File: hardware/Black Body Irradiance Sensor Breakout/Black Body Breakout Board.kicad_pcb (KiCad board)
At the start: 2 copper layers, 15 x 13 mm, 6 parts, among them J2 Conn_01x05, U1 TSL25911FN

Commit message: actual irrad board update
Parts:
- moved C1 3.26 mm to (133.2, 72.8)
- moved R3 2.47 mm to (130.7, 71.3), turned to -90 degrees
- moved R2 1.82 mm to (125.5, 71.4)
- moved U1 1.69 mm to (128.1, 72.9)
- moved R1 0.34 mm to (123.3, 73.2)
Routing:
- net +3V3: track 3.93 -> 0.00 mm, vias 2 -> 0
- net Net-(J2-Pin_3): track 10.3 -> 7.15 mm
- net Net-(J2-Pin_4): track 8.38 -> 6.76 mm, vias 2 -> 1
- net Net-(J2-Pin_5): track 6.66 -> 7.81 mm

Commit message: updated irrad board
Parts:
- moved R2 2.70 mm to (127.5, 69.5)
- moved R3 0.55 mm to (130.8, 71.8), turned to 90 degrees
- moved C1 0.50 mm to (133.8, 72.8)
- moved R1 0.48 mm to (123.7, 72.9), turned to 0 degrees
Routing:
- net Net-(J2-Pin_3): track 7.15 -> 13.0 mm, vias 0 -> 1
- net +3V3: track 0.00 -> 5.43 mm
- net Net-(J2-Pin_4): track 6.76 -> 7.91 mm
- net GND: track 10.2 -> 10.9 mm, vias 2 -> 0
- net Net-(J2-Pin_5): track 7.81 -> 7.80 mm, vias 0 -> 1

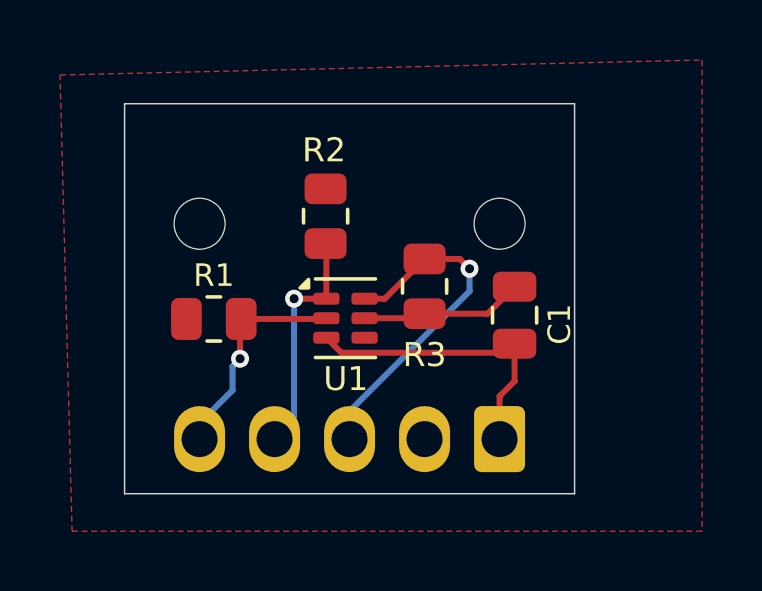
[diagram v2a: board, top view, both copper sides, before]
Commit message: updated fuse silkscreen, added open circuit to TC
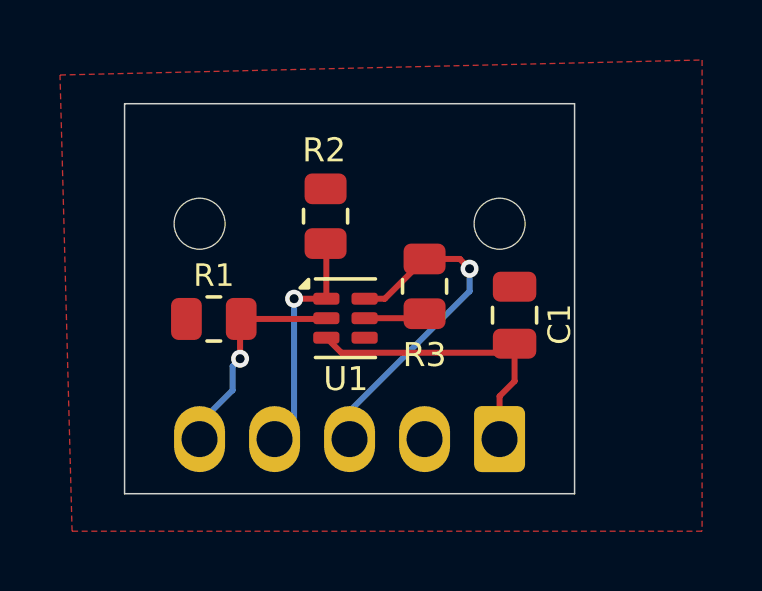
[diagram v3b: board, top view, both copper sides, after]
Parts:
- R2, R3: value 1.5k -> 10k
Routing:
- net +3V3: track 5.43 -> 2.06 mm
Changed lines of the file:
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@@
 			)
 		)
-		(property "Value" "1.5k"
+		(property "Value" "10k"
 			(at 0 1.65 90)
 			(layer "F.Fab")
@@
 			)
 		)
-		(property "Value" "1.5k"
+		(property "Value" "10k"
 			(at 0 1.65 90)
 			(layer "F.Fab")
@@
 		(width 0.2)
 		(layer "F.Cu")
-		(net 1)
-	)
-	(segment
-		(start 130.75 72.75)
-		(end 132.85 72.75)
-		(width 0.2)
-		(layer "F.Cu")
-		(net 1)
-	)
-	(segment
-		(start 132.85 72.75)
-		(end 133.75 71.85)
-		(width 0.2)
-		(layer "F.Cu")

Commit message: updated cap
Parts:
- C1: footprint Capacitor_SMD:C_0805_2012Metric -> Capacitor_SMD:C_0201_0603Metric_Pad0.64x0.40mm_HandSolder
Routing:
- net GND: track 10.9 -> 11.5 mm
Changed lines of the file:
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@@
+			)
+		)
+		(property "LCSC" "C25804"
+			(at 0 0 0)
+			(layer "F.SilkS")
+			(hide yes)
+			(effects
+				(font
+					(size 1.27 1.27)
+					(thickness 0.15)
+				)
 			)
 		)
@@
 			)
 		)
+		(property "LCSC" "C25804"
+			(at 0 0 0)
+			(layer "F.SilkS")
+			(hide yes)
+			(effects
+				(font
+					(size 1.27 1.27)
+					(thickness 0.15)
+				)
+			)
+		)
 		(property ki_fp_filters "R_*")
 		(sheetname "/")
@@
 			)
 		)
+		(property "LCSC" "C25804"
+			(at 0 0 0)
+			(layer "F.SilkS")
+			(hide yes)
+			(effects
+				(font
+					(size 1.27 1.27)
+					(thickness 0.15)
+				)
+			)
+		)
 		(property ki_fp_filters "R_*")
 		(sheetname "/")
@@
 		)
 	)
-	(footprint "Capacitor_SMD:C_0805_2012Metric"
+	(footprint "Capacitor_SMD:C_0201_0603Metric_Pad0.64x0.40mm_HandSolder"
 		(layer "F.Cu")
 		(at 133.75 72.8 90)
-		(descr "Capacitor SMD 0805 (2012 Metric), square (rectangular) end terminal, IPC-7351 nominal, (Body size source: IPC-SM-782 page 76, https://www.pcb-3d.com/wordpress/wp-content/uploads/ipc-sm-782a_amendment_1_and_2.pdf, https://docs.google.com/spreadsheets/d/1BsfQQcO9C6DZCsRaXUlFlo91Tg2WpOkGARC1WS5S8t0/edit?usp=sharing), generated with kicad-footprint-generator")
-		(tags "capacitor")
+		(descr "Capacitor SMD 0201 (0603 Metric), square (rectangular) end terminal, IPC-7351 nominal with elongated pad for handsoldering. (Body size source: https://www.vishay.com/docs/20052/crcw0201e3.pdf), generated with kicad-footprint-generator")
+		(tags "capacitor handsolder")
 		(property "Reference" "C1"
-			(at -0.3 1.5 90)
+			(at 0.04 -0.96 90)
 			(layer "F.SilkS")
 			(effects
 				(font
-					(size 0.75 0.75)
+					(size 1 1)
 					(thickness 0.15)
 				)
@@
 		)
 		(property "Value" "1uF"
-			(at 0 1.68 90)
+			(at 0 1.05 90)
 			(layer "F.Fab")
 			(effects
@@
 			(at 0 0 90)
 			(layer "F.Fab")
+			(hide yes)
+			(effects
+				(font
+					(size 1.27 1.27)
+					(thickness 0.15)
+				)
+			)
+		)
+		(property "LCSC" "C15849"
+			(at 0 0 0)
+			(layer "F.SilkS")
 			(hide yes)
 			(effects
@@
 		(attr smd)
 		(fp_line
-			(start -0.261252 -0.735)
-			(end 0.261252 -0.735)
-			(stroke
-				(width 0.12)
-				(type solid)
-			)
-			(layer "F.SilkS")
-		)
-		(fp_line
-			(start -0.261252 0.735)
-			(end 0.261252 0.735)
-			(stroke
-				(width 0.12)
-				(type solid)
-			)
-			(layer "F.SilkS")
-		)
-		(fp_line
-			(start 1.7 -0.98)
-			(end 1.7 0.98)
-			(stroke
-				(width 0.05)
-				(type solid)
-			)
-			(layer "F.CrtYd")
-		)
-		(fp_line
-			(start -1.7 -0.98)
-			(end 1.7 -0.98)
-			(stroke
-				(width 0.05)
-				(type solid)
-			)
-			(layer "F.CrtYd")
-		)
-		(fp_line
-			(start 1.7 0.98)
-			(end -1.7 0.98)
-			(stroke
-				(width 0.05)
-				(type solid)
-			)
-			(layer "F.CrtYd")
-		)
-		(fp_line
-			(start -1.7 0.98)
-			(end -1.7 -0.98)
-			(stroke
-				(width 0.05)
-				(type solid)
-			)
-			(layer "F.CrtYd")
-		)
-		(fp_line
-			(start 1 -0.625)
-			(end 1 0.625)
-			(stroke
-				(width 0.1)
-				(type solid)
-			)
-			(layer "F.Fab")
-		)
-		(fp_line
-			(start -1 -0.625)
-			(end 1 -0.625)
-			(stroke
-				(width 0.1)
-				(type solid)
-			)
-			(layer "F.Fab")
-		)
-		(fp_line
-			(start 1 0.625)
-			(end -1 0.625)
-			(stroke
-				(width 0.1)
-				(type solid)
-			)
-			(layer "F.Fab")
-		)
-		(fp_line
-			(start -1 0.625)
-			(end -1 -0.625)
+			(start 0.88 -0.35)
+			(end 0.88 0.35)
+			(stroke
+				(width 0.05)
+				(type solid)
+			)
+			(layer "F.CrtYd")
+		)
+		(fp_line
+			(start -0.88 -0.35)
+			(end 0.88 -0.35)
+			(stroke
+				(width 0.05)
+				(type solid)
+			)
+			(layer "F.CrtYd")
+		)
+		(fp_line
+			(start 0.88 0.35)
+			(end -0.88 0.35)
+			(stroke
+				(width 0.05)
+				(type solid)
+			)
+			(layer "F.CrtYd")
+		)
+		(fp_line
+			(start -0.88 0.35)
+			(end -0.88 -0.35)
+			(stroke
+				(width 0.05)
+				(type solid)
+			)
+			(layer "F.CrtYd")
+		)
+		(fp_line
+			(start 0.3 -0.15)
+			(end 0.3 0.15)
+			(stroke
+				(width 0.1)
+				(type solid)
+			)
+			(layer "F.Fab")
+		)
+		(fp_line
+			(start -0.3 -0.15)
+			(end 0.3 -0.15)
+			(stroke
+				(width 0.1)
+				(type solid)
+			)
+			(layer "F.Fab")
+		)
+		(fp_line
+			(start 0.3 0.15)
+			(end -0.3 0.15)
+			(stroke
+				(width 0.1)
+				(type solid)
+			)
+			(layer "F.Fab")
+		)
+		(fp_line
+			(start -0.3 0.15)
+			(end -0.3 -0.15)
 			(stroke
 				(width 0.1)
@@
 		)
 		(fp_text user "${REFERENCE}"
-			(at 0 0 90)
-			(layer "F.Fab")
-			(effects
-				(font
-					(size 0.5 0.5)
-					(thickness 0.08)
-				)
-			)
+			(at 0 -0.68 90)
+			(layer "F.Fab")
+			(effects
+				(font
+					(size 0.25 0.25)
+					(thickness 0.04)
+				)
+			)
+		)
+		(pad "" smd roundrect
+			(at -0.4325 0 90)
+			(size 0.458 0.36)
+			(layers "F.Paste")
+			(roundrect_rratio 0.25)
+		)
+		(pad "" smd roundrect
+			(at 0.4325 0 90)
+			(size 0.458 0.36)
+			(layers "F.Paste")
+			(roundrect_rratio 0.25)
 		)
 		(pad "1" smd roundrect
-			(at -0.95 0 90)
-			(size 1 1.45)
-			(layers "F.Cu" "F.Mask" "F.Paste")
+			(at -0.4075 0 90)
+			(size 0.635 0.4)
+			(layers "F.Cu" "F.Mask")
 			(roundrect_rratio 0.25)
 			(net 2 "GND")
@@
 		)
 		(pad "2" smd roundrect
-			(at 0.95 0 90)
-			(size 1 1.45)
-			(layers "F.Cu" "F.Mask" "F.Paste")
+			(at 0.4075 0 90)
+			(size 0.635 0.4)
+			(layers "F.Cu" "F.Mask")
 			(roundrect_rratio 0.25)
 			(net 1 "+3V3")
@@
 		)
 		(embedded_fonts no)
-		(model "${KICAD9_3DMODEL_DIR}/Capacitor_SMD.3dshapes/C_0805_2012Metric.step"
+		(model "${KICAD9_3DMODEL_DIR}/Capacitor_SMD.3dshapes/C_0201_0603Metric.step"
 			(offset
 				(xyz 0 0 0)
@@
 			(unlocked yes)
 			(layer "F.Fab")
+			(hide yes)
+			(effects
+				(font
+					(size 1.27 1.27)
+					(thickness 0.15)
+				)
+			)
+		)
+		(property "LCSC" "C176812"
+			(at 0 0 0)
+			(layer "F.SilkS")
 			(hide yes)
 			(effects
@@
 	)
 	(segment
+		(start 133.75 75)
+		(end 133.75 73.2075)
+		(width 0.2)
+		(layer "F.Cu")
+		(net 2)
+	)
+	(segment
 		(start 133.25 75.5)
 		(end 133.75 75)
+		(width 0.2)
+		(layer "F.Cu")
+		(net 2)
+	)
+	(segment
+		(start 133.25 76.93)
+		(end 133.25 75.5)
+		(width 0.2)
+		(layer "F.Cu")
+		(net 2)
+	)
+	(segment
+		(start 127.976 74.051)
+		(end 132.9065 74.051)
+		(width 0.2)
+		(layer "F.Cu")
+		(net 2)
+	)
+	(segment
+		(start 132.9065 74.051)
+		(end 133.75 73.2075)
+		(width 0.2)
+		(layer "F.Cu")
+		(net 2)
+	)
+	(segment
+		(start 133.45 76.9)
+		(end 133.45 77.08)
 		(width 0.2)
 		(layer "F.Cu")
@@
 	)
 	(segment
-		(start 133.15 73.85)
-		(end 133.25 73.75)
-		(width 0.2)
-		(layer "F.Cu")
-		(net 2)
-	)
-	(segment
-		(start 133.75 75)
-		(end 133.75 73.75)
-		(width 0.2)
-		(layer "F.Cu")
-		(net 2)
-	)
-	(segment
-		(start 133.449 74.051)
-		(end 133.75 73.75)
-		(width 0.2)
-		(layer "F.Cu")
-		(net 2)
-	)
-	(segment
-		(start 133.25 76.93)
-		(end 133.25 75.5)
-		(width 0.2)
-		(layer "F.Cu")
-		(net 2)
-	)
-	(segment
-		(start 133.45 76.9)
-		(end 133.45 77.08)
-		(width 0.2)
-		(layer "F.Cu")
-		(net 2)
-	)
-	(segment
 		(start 133.45 77.08)
 		(end 133.13 77.08)
 		(width 0.2)
 		(layer "F.Cu")
-		(net 2)
-	)
-	(segment
-		(start 127.976 74.051)
-		(end 133.449 74.051)
-		(width 0.2)
-		(layer "F.Cu")

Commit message: updated caps
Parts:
- C1: footprint Capacitor_SMD:C_0201_0603Metric_Pad0.64x0.40mm_HandSolder -> Capacitor_SMD:C_0603_1608Metric_Pad1.08x0.95mm_HandSolder
- R1, R2, R3: footprint Resistor_SMD:R_0805_2012Metric -> Resistor_SMD:R_0603_1608Metric_Pad0.98x0.95mm_HandSolder
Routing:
- net GND: track 11.5 -> 10.8 mm
